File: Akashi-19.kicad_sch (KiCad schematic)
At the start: 5 parts, among them J1 Conn_01x04_Socket, J2 Conn_01x20_Socket, J3 Conn_01x20_Socket, SW1 SW_Omron_B3FS, U1 Pico

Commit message: Before auto routing.
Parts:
- added J4: QWIIC, sparkfun_conn:JST04_1MM_RA, symbol Sparkfun_conn:Qwiic_Right_Angle
- J1: value Conn_01x04_Socket -> GROVE I2C
- SW1: value SW_Omron_B3FS -> RESET
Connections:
- net +3.3V: now also J4.3 (Pin_3); no longer J1.3 (Pin_3)
- net GND: now also J4.4 (Pin_4)
- net at J2.1 (Pin_1), U1.1 (GPIO0): no longer J1.2 (Pin_2)
- net at J2.2 (Pin_2), U1.2 (GPIO1): no longer J1.1 (Pin_1)
- net +5V: now reaches J3.1 (Pin_1), U1.40 (VBUS)
- net +5V: now also J1.3 (Pin_3)
- net SDA: now reaches J2.6 (Pin_6), U1.6 (GPIO4)
- net SDA: now also J1.2 (Pin_2), J4.2 (Pin_2)
- net SCL: now reaches J2.7 (Pin_7), U1.7 (GPIO5)
- net SCL: now also J1.1 (Pin_1), J4.1 (Pin_1)
- new net: J4.NC1 (NC), J4.NC2 (NC)

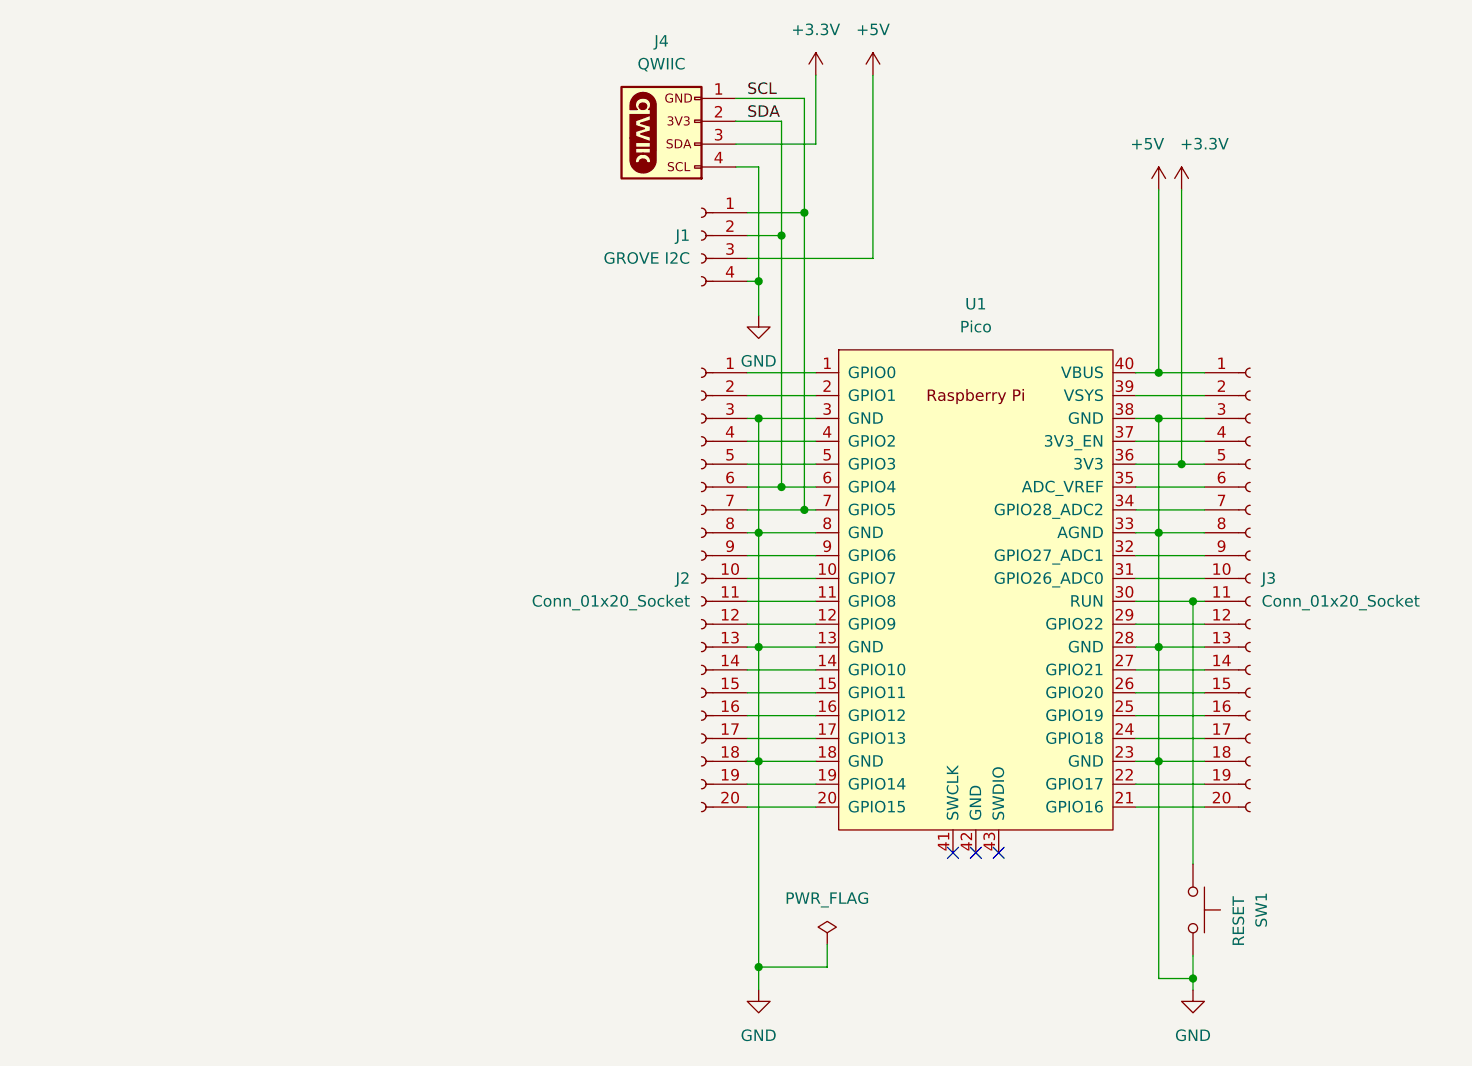
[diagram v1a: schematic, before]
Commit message: Add Serial port and text information.
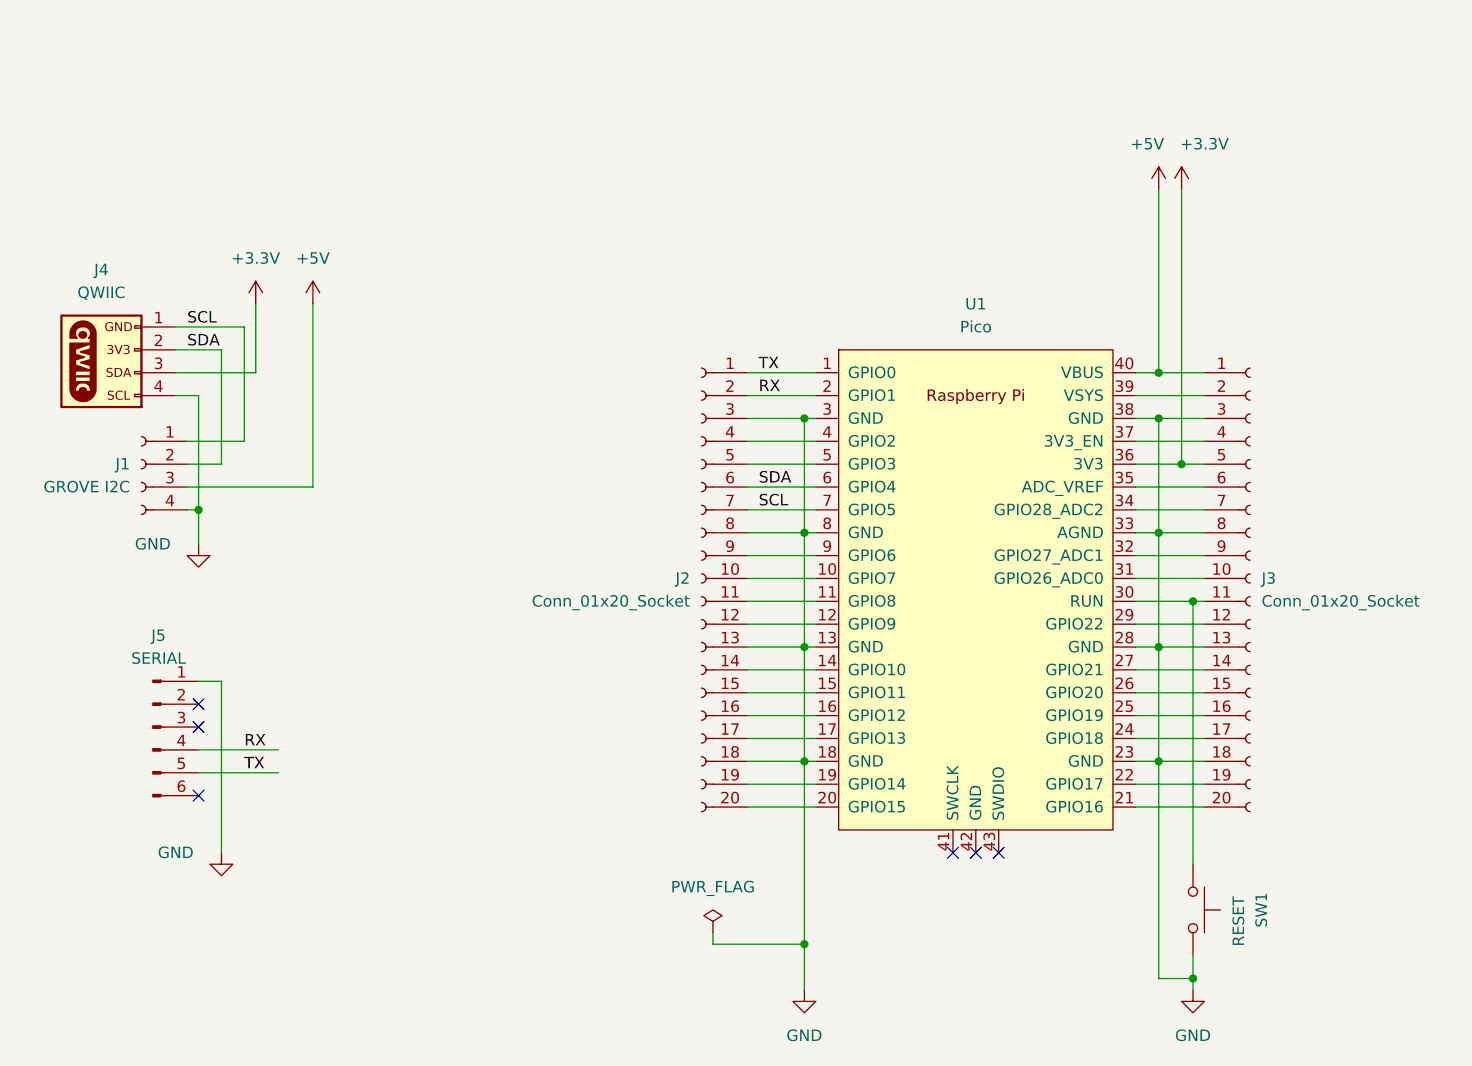
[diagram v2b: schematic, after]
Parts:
- added J5: SERIAL, Connector_PinHeader_2.54mm:PinHeader_1x06_P2.54mm_Horizontal, symbol Connector:Conn_01x06_Pin
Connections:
- net GND: now also J5.1 (Pin_1)
- net TX: now reaches J2.1 (Pin_1), U1.1 (GPIO0)
- net TX: now also J5.5 (Pin_5)
- net RX: now reaches J2.2 (Pin_2), U1.2 (GPIO1)
- net RX: now also J5.4 (Pin_4)
- no-connect marks 3 -> 6
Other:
- moved on the sheet: J1, J4

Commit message: Schematcis was not saved correctly.
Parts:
- U1: value Pico -> Raspberry Pi Pico
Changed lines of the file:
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@@
       (effects (font (size 1.27 1.27)))
     )
-    (property "Value" "Pico" (at 152.4 72.39 0)
+    (property "Value" "Raspberry Pi Pico" (at 152.4 72.39 0)
       (effects (font (size 1.27 1.27)))
     )

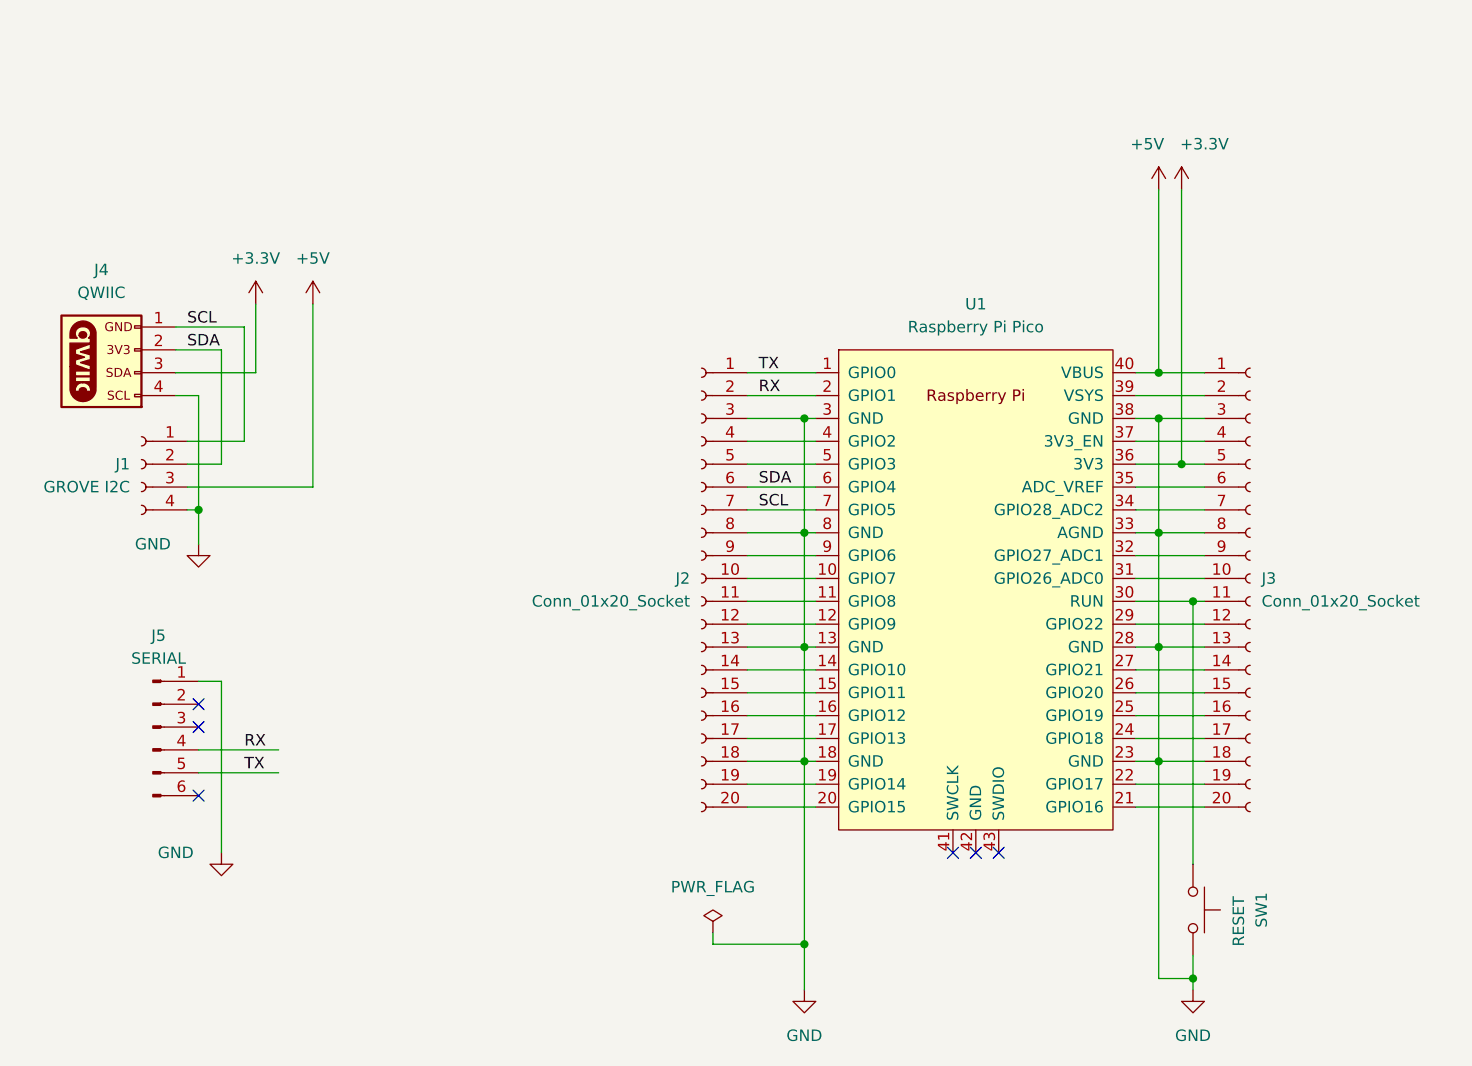
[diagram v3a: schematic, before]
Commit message: Renumbered J1, J2, J3.
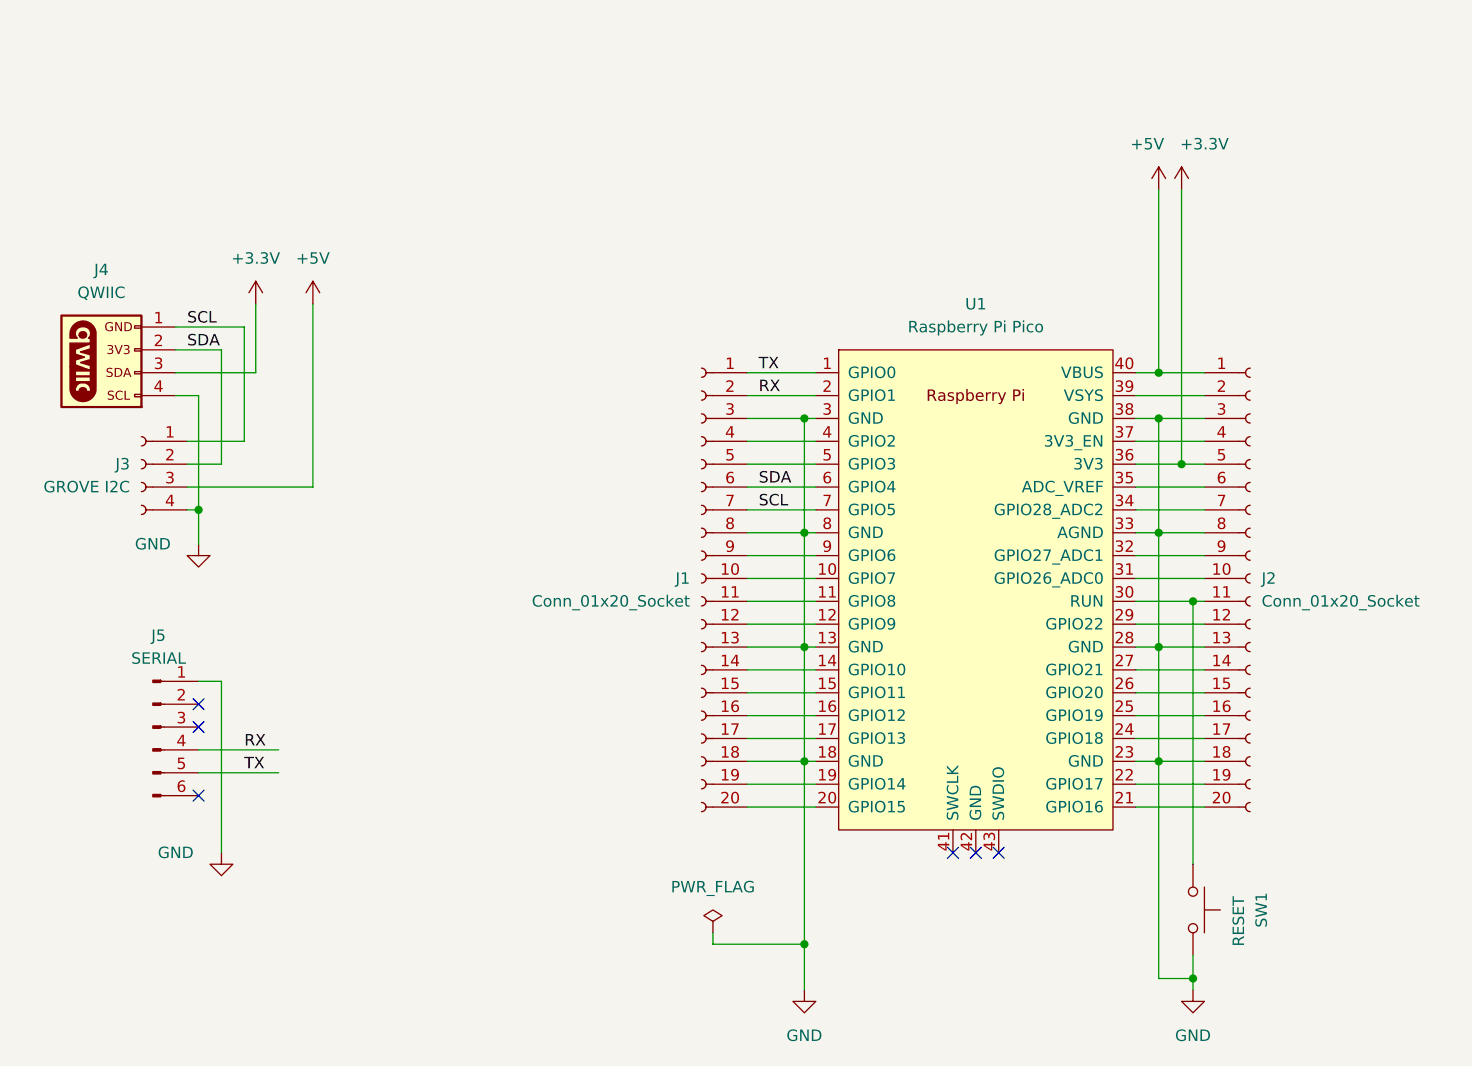
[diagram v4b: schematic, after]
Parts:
- renumbered J2 to J1, J3 to J2, J1 to J3
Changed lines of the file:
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@@
   (symbol (lib_id "Connector:Conn_01x20_Socket") (at 121.92 100.33 0) (mirror y) (unit 1)
     (in_bom yes) (on_board yes) (dnp no)
-    (property "Reference" "J2" (at 120.65 100.33 0)
+    (property "Reference" "J1" (at 120.65 100.33 0)
       (effects (font (size 1.27 1.27)) (justify left))
     )
@@
       (project "Akashi-19"
         (path "/f285b53a-63c1-49f6-9ada-34701b701936"
-          (reference "J2") (unit 1)
+          (reference "J1") (unit 1)
         )
       )
@@
   (symbol (lib_id "Connector:Conn_01x04_Socket") (at 59.69 87.63 0) (mirror y) (unit 1)
     (in_bom yes) (on_board yes) (dnp no)
-    (property "Reference" "J1" (at 58.42 87.63 0)
+    (property "Reference" "J3" (at 58.42 87.63 0)
       (effects (font (size 1.27 1.27)) (justify left))
     )
@@
       (project "Akashi-19"
         (path "/f285b53a-63c1-49f6-9ada-34701b701936"
-          (reference "J1") (unit 1)
+          (reference "J3") (unit 1)
         )
       )
@@
   (symbol (lib_id "Connector:Conn_01x20_Socket") (at 182.88 100.33 0) (unit 1)
     (in_bom yes) (on_board yes) (dnp no) (fields_autoplaced)
-    (property "Reference" "J3" (at 184.15 100.33 0)
+    (property "Reference" "J2" (at 184.15 100.33 0)
       (effects (font (size 1.27 1.27)) (justify left))
     )
@@
       (project "Akashi-19"
         (path "/f285b53a-63c1-49f6-9ada-34701b701936"
-          (reference "J3") (unit 1)
-        )
-      )
+          (reference "J2") (unit 1)
+        )
+      )

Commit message: Correct the wrong connection of Qwiic.
The connection was right-side-left.
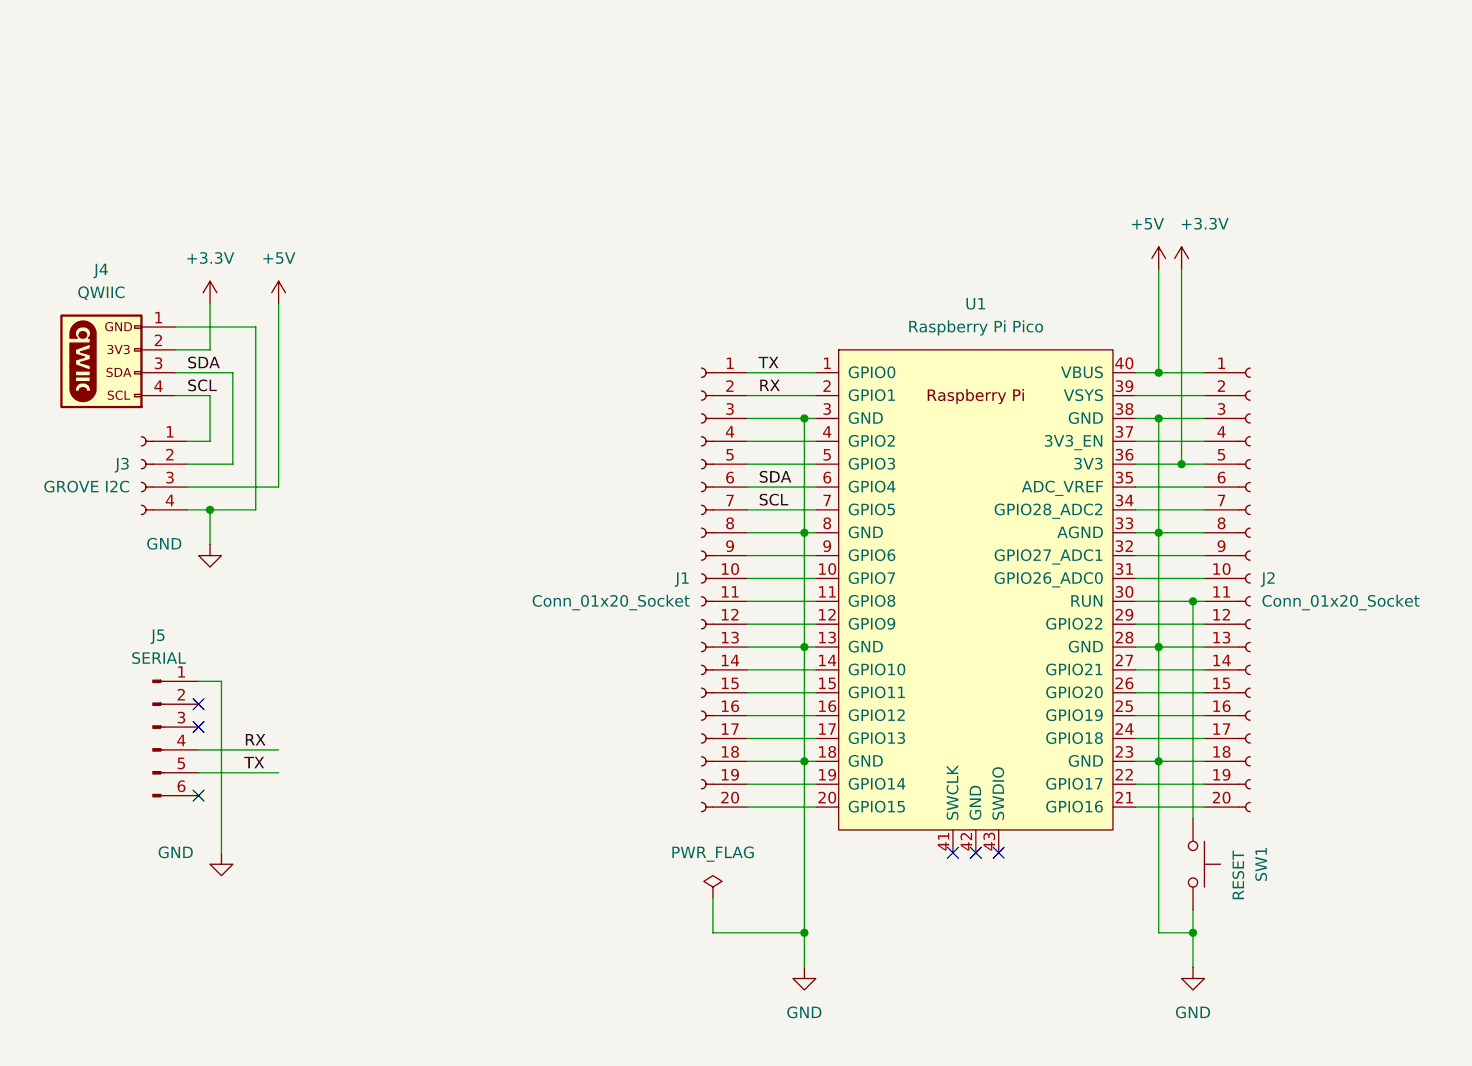
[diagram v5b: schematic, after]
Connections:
- net +3.3V: now also J4.2 (Pin_2); no longer J4.3 (Pin_3)
- net GND: now also J4.1 (Pin_1); no longer J4.4 (Pin_4)
- net SCL: now also J4.4 (Pin_4); no longer J4.1 (Pin_1)
- net SDA: now also J4.3 (Pin_3); no longer J4.2 (Pin_2)
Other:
- moved on the sheet: SW1

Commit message: Refine the wires for the signal integrity.
- Connect GND pin of SWD.
- Move some wire to give the space to GND.
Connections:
- net GND: now also U1.42 (GND)
- no-connect marks 6 -> 5
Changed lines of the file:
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@@
   )
   (no_connect (at 66.04 116.84))
-  (no_connect (at 152.4 130.81))
   (no_connect (at 66.04 114.3))
   (no_connect (at 149.86 130.81))
@@
   )
   (wire (pts (xy 133.35 107.95) (xy 133.35 120.65))
+    (stroke (width 0) (type default))
+  )
+  (wire (pts (xy 152.4 143.51) (xy 152.4 130.81))
     (stroke (width 0) (type default))
   )
@@
         )
       )
+    )
+  )
+  (symbol (lib_id "power:GND") (at 152.4 143.51 0) (unit 1)
+    (in_bom yes) (on_board yes) (dnp no) (fields_autoplaced)
+    (property "Reference" "#PWR09" (at 152.4 149.86 0)
+      (effects (font (size 1.27 1.27)) hide)
+    )
+    (property "Value" "GND" (at 152.4 148.59 0)
+      (effects (font (size 1.27 1.27)))
+    )
+    (property "Footprint" "" (at 152.4 143.51 0)
+      (effects (font (size 1.27 1.27)) hide)
+    )
+    (property "Datasheet" "" (at 152.4 143.51 0)
+      (effects (font (size 1.27 1.27)) hide)
+    )
+    (pin "1")
+    (instances
+      (project "Akashi-19"
+        (path "/f285b53a-63c1-49f6-9ada-34701b701936"
+          (reference "#PWR09") (unit 1)
+        )
+      )
